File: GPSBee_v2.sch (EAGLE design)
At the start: 60 parts, among them J1 MICRO-USB-5P-340015001, U1 UBLOX-LEA-6T, U2 TPS73633, U3 TPS73633, X1 SERIAL, X2 ANT, X3 FOUT, X4 ANT, X5 FOUT, X6 1PPS, X7 PC, X8 1PPS, X9 22-23-2021

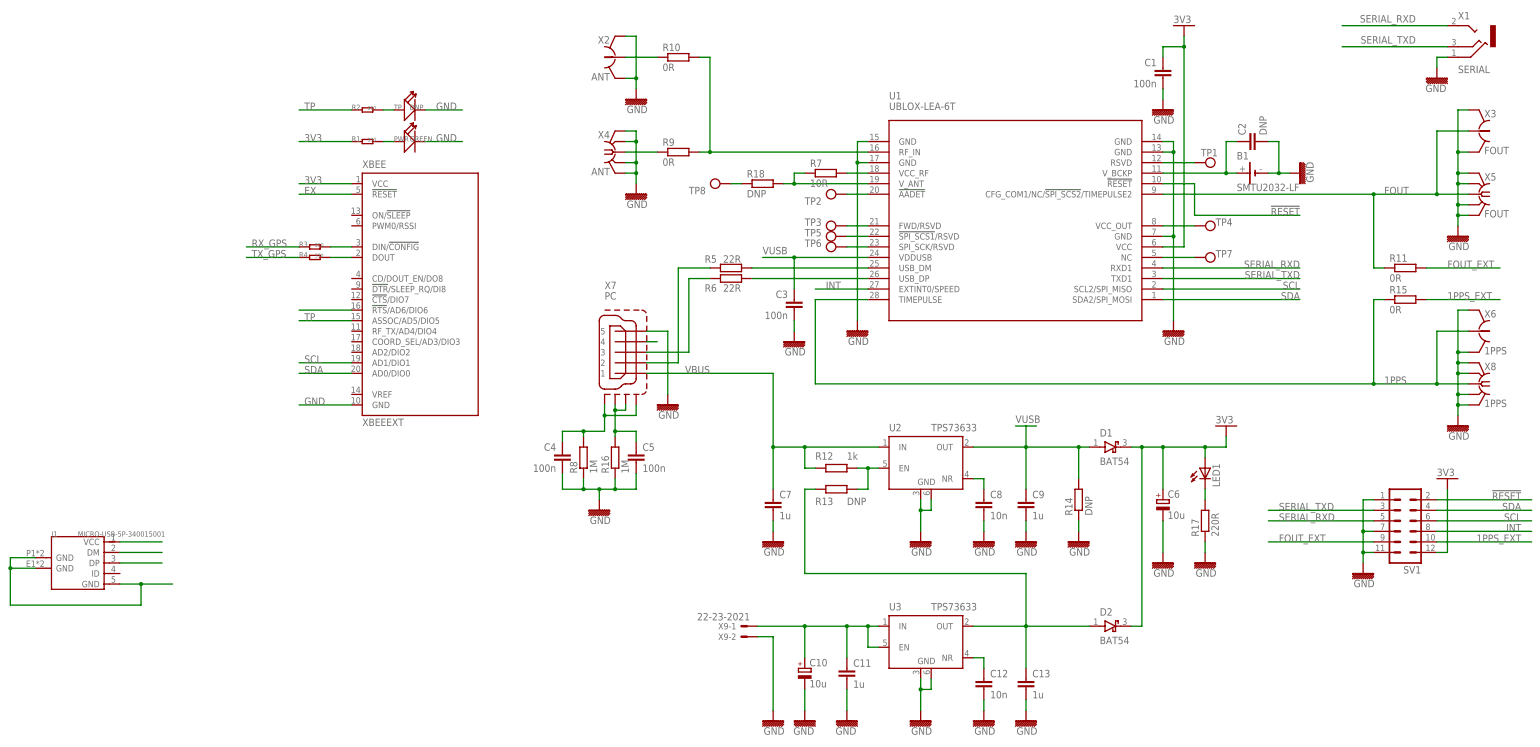
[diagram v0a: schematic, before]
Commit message: Pulled in design from osmo-lea-6T board
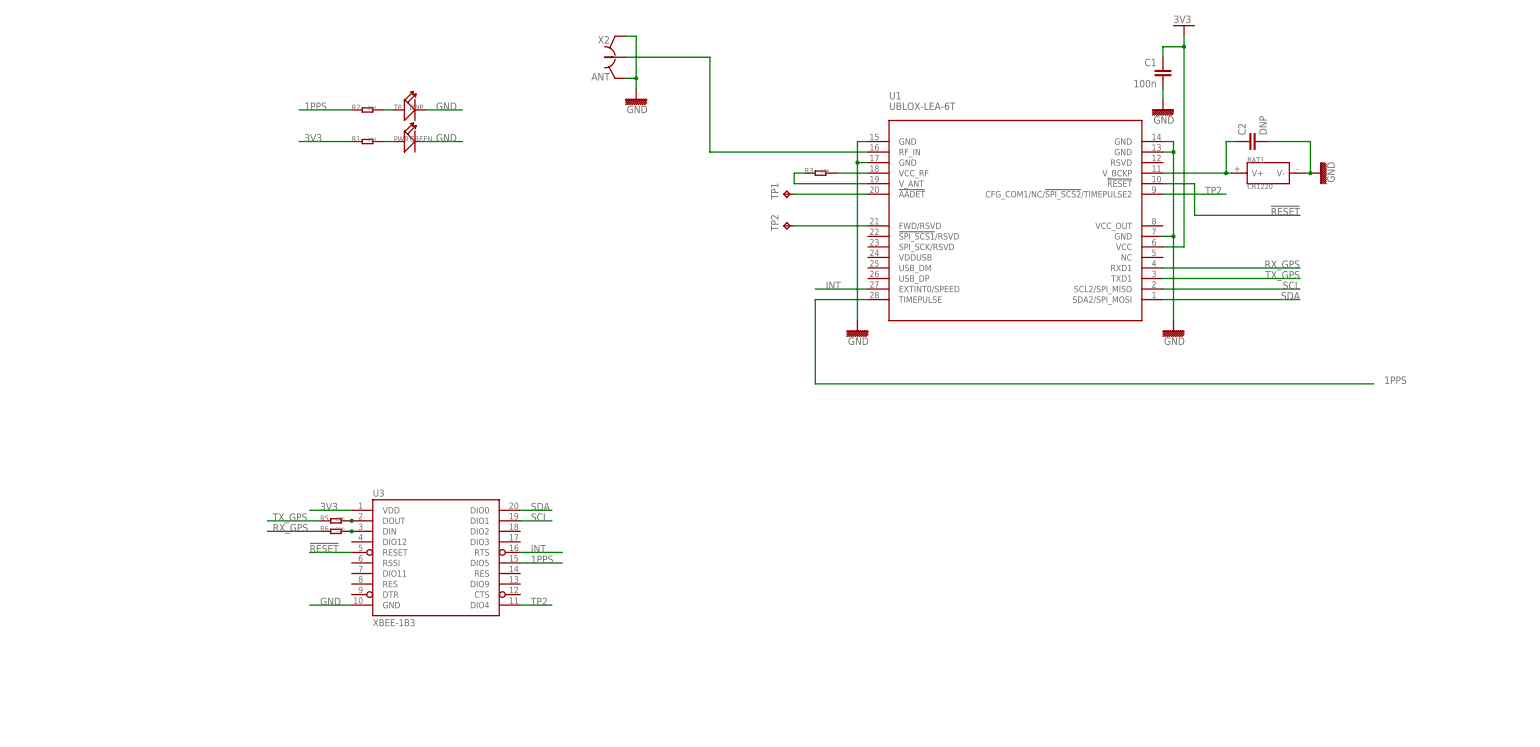
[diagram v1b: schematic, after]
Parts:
- removed B1: SMTU2032-LF, we_misc:BA2032SMD
- removed C10, C6: 10u, rcl:CPOL-EUA/3216-18R
- removed C11, C13, C7, C9: 1u, we_passive:C-EU_0603
- removed C12, C8: 10n, we_passive:C-EU_0603
- removed C3, C4, C5: 100n, we_passive:C-EU_0603
- removed D1, D2: BAT54, we_passive:D_SCHOTTKY_SOT23
- removed J1: MICRO-USB-5P-340015001, Connector:MICRO-USB-5P-340015001
- removed LED1: (no value), led:LEDSML0603
- removed R10, R11, R15, R9: 0R, we_passive:R-EU_0603
- removed R12: 1k, we_passive:R-EU_0603
- removed R13, R14, R18: DNP, we_passive:R-EU_0603
- removed R16, R8: 1M, we_passive:R-EU_0603
- removed R17: 220R, we_passive:R-EU_0603
- removed R4: 330, Discrete:R-0603
- removed R7: 10R, we_passive:R-EU_0603
- removed SV1: (no value), con-lstb-tnt:MA06-2
- removed TP3, TP4, TP5, TP6, TP7, TP8: TESTPAD, we_conn:TESTPAD
- removed U2: TPS73633, laforge:TPS736XX
- removed X1: SERIAL, laforge:JACK2.5_SJ-2523
- removed X3: FOUT, we_conn:HRS_UFL
- removed X4: ANT, we_conn:SMA-F-S-EDGE
- removed X5: FOUT, we_conn:SMA-F-S-EDGE
- removed X6: 1PPS, we_conn:HRS_UFL
- removed X7: PC, con-hirose:MINI-USB-SHIELD-UX60-MB-5ST
- removed X8: 1PPS, we_conn:SMA-F-S-EDGE
- removed X9: 22-23-2021, con-molex:22-23-2021
- removed XBEE: XBEEEXT, EXT_moudle:XBEEEXT
- added BAT1: CR1220, Connector:BAT-HOLDER-SMD-1220
- R3: value 330 -> 10R
- R5, R6: value 22R -> 330; device we_passive:R-EU_0603 -> Discrete:R-0603
- TP1, TP2: value TESTPAD -> TPTP10R; device we_conn:TESTPAD -> testpad:TPTP10R
- U3: value TPS73633 -> XBEE-1B3; device laforge:TPS736XX -> SparkFun-RF:XBEE-1B3
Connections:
- removed net 1PPS_EXT: R15.2, SV1.10
- removed net EX: XBEE.!RESET
- removed net FOUT: R11.1, U1.CFG_COM1/NC/!SPI_SCS2!/TIMEPULSE2, X3.1, X5.1
- removed net FOUT_EXT: R11.2, SV1.9
- removed net N$10: J1.DM
- removed net N$11: J1.DP
- removed net N$12: J1.GND@1, J1.GND@2, J1.GND@3
- removed net N$13: R6.1, X7G$1.3
- removed net N$14: R5.1, X7G$1.2
- removed net N$17: TP3.TP, U1.FWD/RSVD
- removed net N$18: TP5.TP, U1.!SPI_SCS1!/RSVD
- removed net N$19: TP6.TP, U1.SPI_SCK/RSVD
- removed net N$20: R10.1, X2.1
- removed net N$22: TP1.TP, U1.RSVD
- removed net N$23: TP4.TP, U1.VCC_OUT
- removed net N$24: TP7.TP, U1.NC
- removed net N$25: R9.1, X4.1
- removed net N$27: TP2.TP, U1.!AADET
- removed net N$28: C10.+, C11.1, U3.EN, U3.IN, X9-1.S
- removed net N$29: C12.1, U3.NR
- removed net N$30: C13.1, D2.A, R13.1, U3.OUT
- removed net N$31: R12.2, R13.2, U2.EN
- removed net N$32: C8.1, U2.NR
- removed net N$33: C4.1, R8.2, X7S.S1, X7S.S4
- removed net N$34: C5.1, R16.2, X7S.S2, X7S.S3
- removed net N$35: LED1.C, R17.2
- removed net N$36: R18.1, TP8.TP
- removed net N$7: R6.2, U1.USB_DP
- removed net N$8: XBEE.!RTS!/AD6/DIO6
- removed net N$9: J1.VCC
- removed net SERIAL_RXD: SV1.5, U1.RXD1, X1.TIP
- removed net SERIAL_TXD: SV1.3, U1.TXD1, X1.MIDDLE
- removed net TP: R2.1, XBEE.ASSOC/AD5/DIO5
- removed net VBUS: C7.1, R12.1, U2.IN, X7G$1.1
- removed net VUSB: C3.1, C9.1, D1.A, R14.2, U1.VDDUSB, U2.OUT
- new net TP2: U1.CFG_COM1/NC/!SPI_SCS2!/TIMEPULSE2, U3.DIO4
- net !RESET: now also U3.RESET; no longer SV1.2
- net 1PPS: now also R2.1, U3.DIO5; no longer R15.1, X6.1, X8.1
- net 3V3: now also U3.VDD; no longer C6.+, D1.C, D2.C, LED1.A, SV1.12, XBEE.VCC
- net GND: now also BAT1.V-; no longer B1.-, C10.-, C11.2, C12.2, C13.2, C3.2, C4.2, C5.2, C6.-, C7.2, C8.2, C9.2, R14.1, R16.1, R17.1, R8.1, SV1.1, SV1.11, SV1.7, U2.GND, U2.GND1, U3.GND1, X1.RING, X3.GND@1, X3.GND@2, X4.GND@1, X4.GND@2, X4.GND@3, X4.GND@4, X5.GND@1, X5.GND@2, X5.GND@3, X5.GND@4, X6.GND@1, X6.GND@2, X7G$1.5, X8.GND@1, X8.GND@2, X8.GND@3, X8.GND@4, X9-2.S, XBEE.GND
- net INT: now also U3.RTS; no longer SV1.8
- net N$15: now also R3.2; no longer R7.2
- net N$16: now also R3.1; no longer R18.2, R7.1
- net N$2: now also R6.2, U3.DIN; no longer X7G$1.4
- net N$21: now also BAT1.V+; no longer B1.+
- net N$26: now also X2.1; no longer R10.2, R9.2
- net N$3: now also TP1.TP, U1.!AADET; no longer R5.2, U1.USB_DM
- net N$4: now also R5.2, U3.DOUT; no longer R3.2, XBEE.DIN/!CONFIG
- net N$6: now also TP2.TP, U1.FWD/RSVD; no longer R4.2, XBEE.DOUT
- net RX_GPS: now also R6.1, U1.RXD1; no longer R3.1
- net SCL: now also U3.DIO1; no longer SV1.6, XBEE.AD1/DIO1
- net SDA: now also U3.DIO0; no longer SV1.4, XBEE.AD0/DIO0
- net TX_GPS: now also R5.1, U1.TXD1; no longer R4.1
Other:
- moved on the sheet: R3

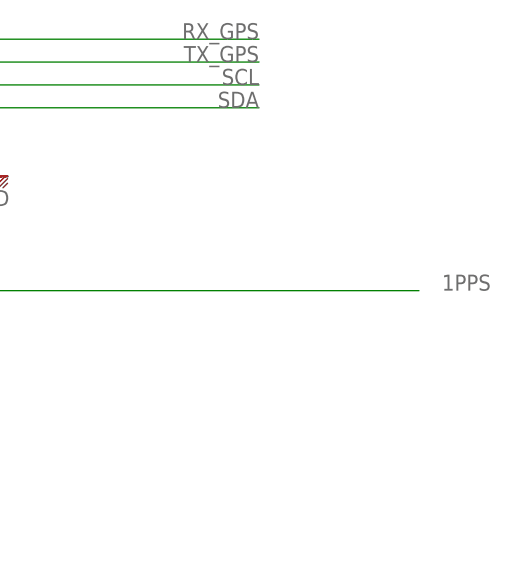
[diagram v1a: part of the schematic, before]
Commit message: Changed DRU and added new frame
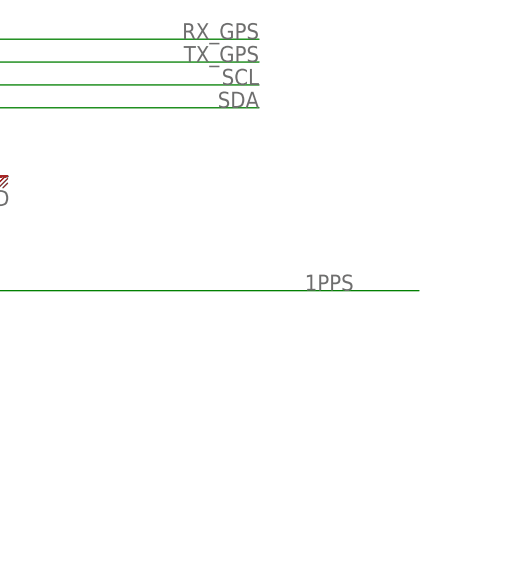
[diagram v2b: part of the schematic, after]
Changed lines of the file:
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@@
 <grid distance="0.1" unitdist="inch" unit="inch" style="lines" multiple="1" display="no" altdistance="0.01" altunitdist="inch" altunit="inch"/>
 <layers>
-<layer number="1" name="Top" color="4" fill="1" visible="yes" active="no"/>
-<layer number="2" name="Route2" color="1" fill="3" visible="yes" active="no"/>
-<layer number="3" name="Route3" color="4" fill="3" visible="yes" active="no"/>
-<layer number="4" name="Route4" color="1" fill="4" visible="yes" active="no"/>
-<layer number="5" name="Route5" color="4" fill="4" visible="yes" active="no"/>
-<layer number="6" name="Route6" color="1" fill="8" visible="yes" active="no"/>
-<layer number="7" name="Route7" color="4" fill="8" visible="yes" active="no"/>
-<layer number="8" name="Route8" color="1" fill="2" visible="yes" active="no"/>
-<layer number="9" name="Route9" color="4" fill="2" visible="yes" active="no"/>
-<layer number="10" name="Route10" color="1" fill="7" visible="yes" active="no"/>
-<layer number="11" name="Route11" color="4" fill="7" visible="yes" active="no"/>
-<layer number="12" name="Route12" color="1" fill="5" visible="yes" active="no"/>
-<layer number="13" name="Route13" color="4" fill="5" visible="yes" active="no"/>
-<layer number="14" name="Route14" color="1" fill="6" visible="yes" active="no"/>
-<layer number="15" name="Route15" color="4" fill="6" visible="yes" active="no"/>
-<layer number="16" name="Bottom" color="1" fill="1" visible="yes" active="no"/>
-<layer number="17" name="Pads" color="2" fill="1" visible="yes" active="no"/>
-<layer number="18" name="Vias" color="2" fill="1" visible="yes" active="no"/>
-<layer number="19" name="Unrouted" color="6" fill="1" visible="yes" active="no"/>
-<layer number="20" name="Dimension" color="5" fill="1" visible="yes" active="no"/>
-<layer number="21" name="tPlace" color="7" fill="1" visible="yes" active="no"/>
-<layer number="22" name="bPlace" color="3" fill="1" visible="yes" active="no"/>
-<layer number="23" name="tOrigins" color="15" fill="1" visible="yes" active="no"/>
-<layer number="24" name="bOrigins" color="3" fill="1" visible="yes" active="no"/>
-<layer number="25" name="tNames" color="7" fill="1" visible="yes" active="no"/>
-<layer number="26" name="bNames" color="3" fill="1" visible="yes" active="no"/>
-<layer number="27" name="tValues" color="7" fill="1" visible="yes" active="no"/>
-<layer number="28" name="bValues" color="7" fill="1" visible="yes" active="no"/>
+<layer number="1" name="Top" color="4" fill="1" visible="no" active="no"/>
+<layer number="2" name="Route2" color="1" fill="3" visible="no" active="no"/>
+<layer number="3" name="Route3" color="4" fill="3" visible="no" active="no"/>
+<layer number="4" name="Route4" color="1" fill="4" visible="no" active="no"/>
+<layer number="5" name="Route5" color="4" fill="4" visible="no" active="no"/>
+<layer number="6" name="Route6" color="1" fill="8" visible="no" active="no"/>
+<layer number="7" name="Route7" color="4" fill="8" visible="no" active="no"/>
+<layer number="8" name="Route8" color="1" fill="2" visible="no" active="no"/>
+<layer number="9" name="Route9" color="4" fill="2" visible="no" active="no"/>
+<layer number="10" name="Route10" color="1" fill="7" visible="no" active="no"/>
+<layer number="11" name="Route11" color="4" fill="7" visible="no" active="no"/>
+<layer number="12" name="Route12" color="1" fill="5" visible="no" active="no"/>
+<layer number="13" name="Route13" color="4" fill="5" visible="no" active="no"/>
+<layer number="14" name="Route14" color="1" fill="6" visible="no" active="no"/>
+<layer number="15" name="Route15" color="4" fill="6" visible="no" active="no"/>
+<layer number="16" name="Bottom" color="1" fill="1" visible="no" active="no"/>
+<layer number="17" name="Pads" color="2" fill="1" visible="no" active="no"/>
+<layer number="18" name="Vias" color="2" fill="1" visible="no" active="no"/>
+<layer number="19" name="Unrouted" color="6" fill="1" visible="no" active="no"/>
+<layer number="20" name="Dimension" color="5" fill="1" visible="no" active="no"/>
+<layer number="21" name="tPlace" color="7" fill="1" visible="no" active="no"/>
+<layer number="22" name="bPlace" color="3" fill="1" visible="no" active="no"/>
+<layer number="23" name="tOrigins" color="15" fill="1" visible="no" active="no"/>
+<layer number="24" name="bOrigins" color="3" fill="1" visible="no" active="no"/>
+<layer number="25" name="tNames" color="7" fill="1" visible="no" active="no"/>
+<layer number="26" name="bNames" color="3" fill="1" visible="no" active="no"/>
+<layer number="27" name="tValues" color="7" fill="1" visible="no" active="no"/>
+<layer number="28" name="bValues" color="7" fill="1" visible="no" active="no"/>
 <layer number="29" name="tStop" color="7" fill="3" visible="no" active="no"/>
 <layer number="30" name="bStop" color="7" fill="6" visible="no" active="no"/>
@@
 <layer number="35" name="tGlue" color="7" fill="4" visible="no" active="no"/>
 <layer number="36" name="bGlue" color="7" fill="5" visible="no" active="no"/>
-<layer number="37" name="tTest" color="7" fill="1" visible="yes" active="no"/>
-<layer number="38" name="bTest" color="7" fill="1" visible="yes" active="no"/>
+<layer number="37" name="tTest" color="7" fill="1" visible="no" active="no"/>
+<layer number="38" name="bTest" color="7" fill="1" visible="no" active="no"/>
 <layer number="39" name="tKeepout" color="4" fill="11" visible="no" active="no"/>
 <layer number="40" name="bKeepout" color="1" fill="11" visible="no" active="no"/>
@@
 <layer number="44" name="Drills" color="7" fill="1" visible="no" active="no"/>
 <layer number="45" name="Holes" color="7" fill="1" visible="no" active="no"/>
-<layer number="46" name="Milling" color="3" fill="1" visible="yes" active="no"/>
-<layer number="47" name="Measures" color="7" fill="1" visible="yes" active="no"/>
-<layer number="48" name="Document" color="7" fill="1" visible="yes" active="no"/>
-<layer number="49" name="Reference" color="7" fill="1" visible="yes" active="no"/>
-<layer number="50" name="dxf" color="7" fill="1" visible="yes" active="no"/>
-<layer number="51" name="tDocu" color="7" fill="1" visible="yes" active="no"/>
-<layer number="52" name="bDocu" color="7" fill="1" visible="yes" active="no"/>
-<layer number="53" name="tGND_GNDA" color="7" fill="9" visible="yes" active="no"/>
-<layer number="54" name="bGND_GNDA" color="1" fill="9" visible="yes" active="no"/>
-<layer number="56" name="wert" color="7" fill="1" visible="yes" active="no"/>
-<layer number="57" name="tCAD" color="7" fill="1" visible="yes" active="no"/>
+<layer number="46" name="Milling" color="3" fill="1" visible="no" active="no"/>
+<layer number="47" name="Measures" color="7" fill="1" visible="no" active="no"/>
+<layer number="48" name="Document" color="7" fill="1" visible="no" active="no"/>
+<layer number="49" name="Reference" color="7" fill="1" visible="no" active="no"/>
+<layer number="50" name="dxf" color="7" fill="1" visible="no" active="no"/>
+<layer number="51" name="tDocu" color="7" fill="1" visible="no" active="no"/>
+<layer number="52" name="bDocu" color="7" fill="1" visible="no" active="no"/>
+<layer number="53" name="tGND_GNDA" color="7" fill="9" visible="no" active="no"/>
+<layer number="54" name="bGND_GNDA" color="1" fill="9" visible="no" active="no"/>
+<layer number="56" name="wert" color="7" fill="1" visible="no" active="no"/>
+<layer number="57" name="tCAD" color="7" fill="1" visible="no" active="no"/>
 <layer number="91" name="Nets" color="2" fill="1" visible="yes" active="yes"/>
 <layer number="92" name="Busses" color="1" fill="1" visible="yes" active="yes"/>
@@
 <schematic xreflabel="%F%N/%S.%C%R" xrefpart="/%S.%C%R">
 <attributes>
+<attribute name="CNAME" value="GPSBee LEA6T"/>
+<attribute name="CREVISION" value="1.0"/>
+<attribute name="DESIGNER" value="Tisham Dhar"/>
 </attributes>
 <variantdefs>
@@
 <part name="TP1" library="testpad" deviceset="TP" device="TP10R" value="TPTP10R"/>
 <part name="TP2" library="testpad" deviceset="TP" device="TP10R"/>
+<part name="FRAME1" library="SparkFun-Aesthetics" deviceset="FRAME-A4L" device=""/>
 </parts>
 <sheets>
 <sheet>
 <plain>
-<frame x1="-104.14" y1="-124.46" x2="327.66" y2="149.86" columns="8" rows="5" layer="91"/>
 </plain>
 <instances>
@@
 <instance part="TP1" gate="G$1" x="101.6" y="53.34" rot="R90"/>
 <instance part="TP2" gate="G$1" x="101.6" y="45.72" rot="R90"/>
+<instance part="FRAME1" gate="G$1" x="-27.94" y="-73.66"/>
 </instances>
 <busses>
@@
 <wire x1="109.22" y1="27.94" x2="109.22" y2="7.62" width="0.1524" layer="91"/>
 <wire x1="109.22" y1="7.62" x2="243.84" y2="7.62" width="0.1524" layer="91"/>
-<label x="246.38" y="7.62" size="1.778" layer="95"/>
-</segment>
-<segment>
+<label x="231.14" y="7.62" size="1.778" layer="95"/>
+</segment>
+<segment>
